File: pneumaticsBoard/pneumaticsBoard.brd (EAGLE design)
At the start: 188 x 25.4 mm, 48 parts, among them IC1 MAX232, Q1 BSS296, Q2 BSS296, Q3 BSS296, Q4 BSS296, Q5 BSS296, Q6 BSS296, Q7 BSS296, Q8 BSS296, U1 ATMEGA328P-PU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

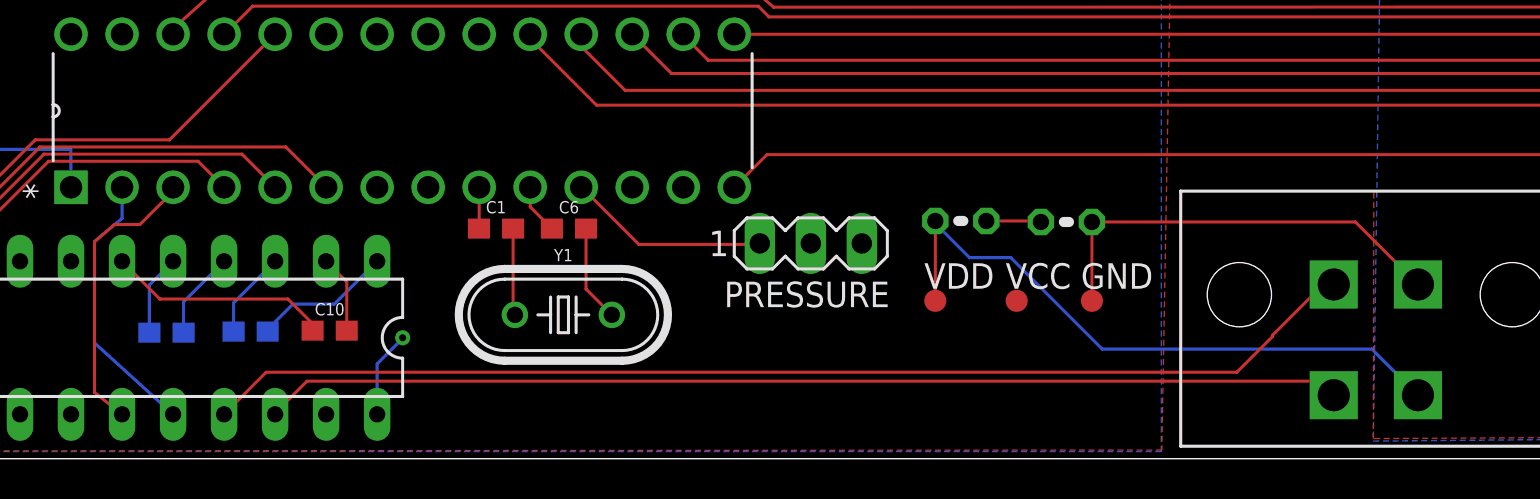
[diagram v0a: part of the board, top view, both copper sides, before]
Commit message: Pneumatics Board complete. Gerber files uploaded.
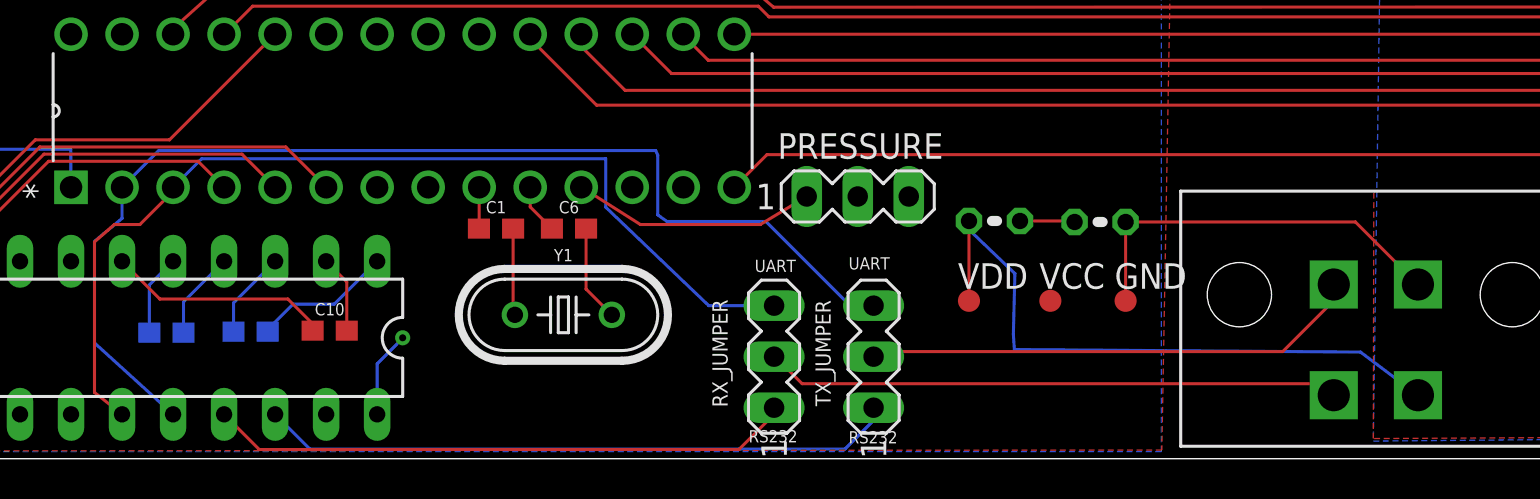
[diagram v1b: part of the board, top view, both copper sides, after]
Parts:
- added RX_JUMPER, TX_JUMPER: (no value), con-lstb:MA03-1
- moved PRESSURE 3.30 mm to (62.0, 13.1)
- moved GND 1.68 mm to (75.3, 7.86)
- moved R4 1.68 mm to (68.8, 11.8)
- moved R6 1.68 mm to (74.0, 11.8)
- moved VCC 1.68 mm to (71.5, 7.86)
- moved VDD 1.68 mm to (67.5, 7.86)
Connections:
- removed net RS232_RX-ATMEGA_TX: IC1.12, U1.2
- removed net RS232_TX-ATMEGA_RX: IC1.11, U1.3
- new net N$16: IC1.13, RX_JUMPER.1
- new net RX_ORIGINAL: RX_JUMPER.2, U$2.P1
- new net TX_ORIGINAL: TX_JUMPER.2, U$2.P3
- net N$3: now also IC1.14, TX_JUMPER.1; no longer R4.1, R6.2
- net RX: now also IC1.12, TX_JUMPER.3, U1.2; no longer IC1.13, U$2.P3
- net TX: now also IC1.11, RX_JUMPER.3, U1.3; no longer IC1.14, U$2.P1
- net VCC: now also R4.1, R6.2
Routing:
- net N$16: track 0.00 -> 29.2 mm
- net N$3: track 2.74 -> 31.7 mm
- net RX_ORIGINAL: track 0.00 -> 28.7 mm
- net TX_ORIGINAL: track 0.00 -> 24.9 mm
- net RS232_TX-ATMEGA_RX: track 14.4 -> 0.00 mm
- net RS232_RX-ATMEGA_TX: track 13.7 -> 0.00 mm
- net TX: track 53.7 -> 49.3 mm
- net VCC: track 4.31 -> 7.05 mm
- net N$6: track 10.1 -> 12.2 mm
- net GND: track 35.4 -> 33.7 mm
- net RX: track 58.0 -> 56.8 mm
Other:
- board text added: "RS232"
- board text added: "UART"

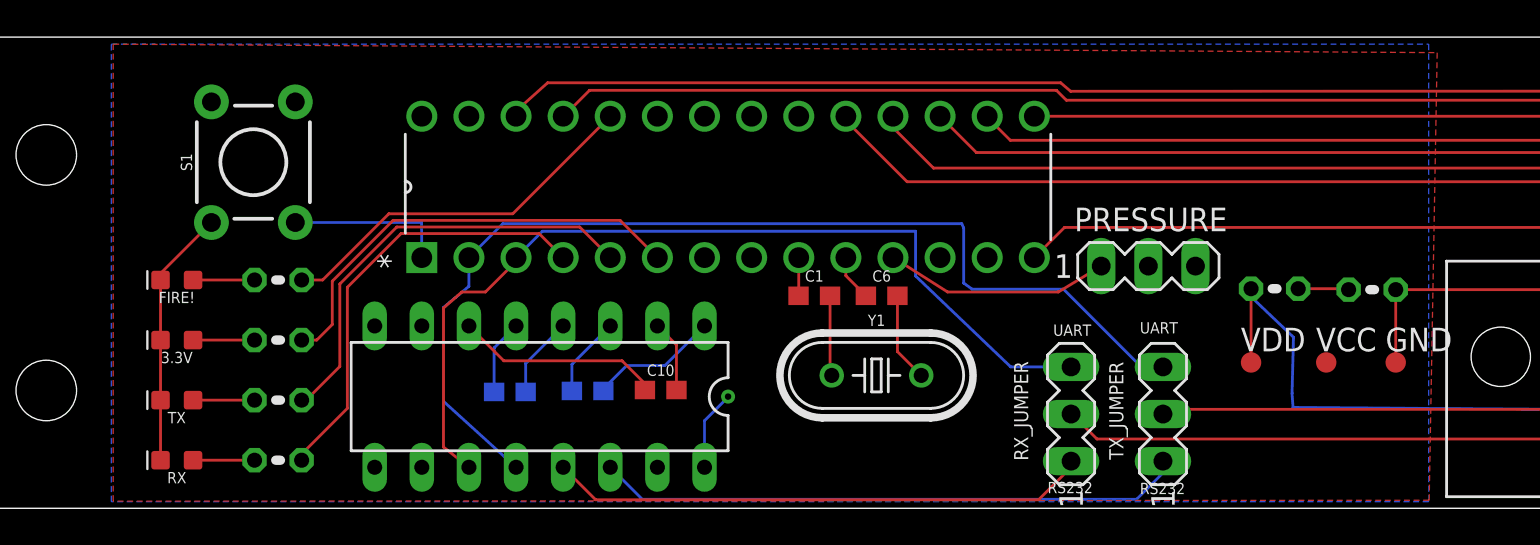
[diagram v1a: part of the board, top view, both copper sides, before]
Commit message: Moved C10, changed GND place on logic side.
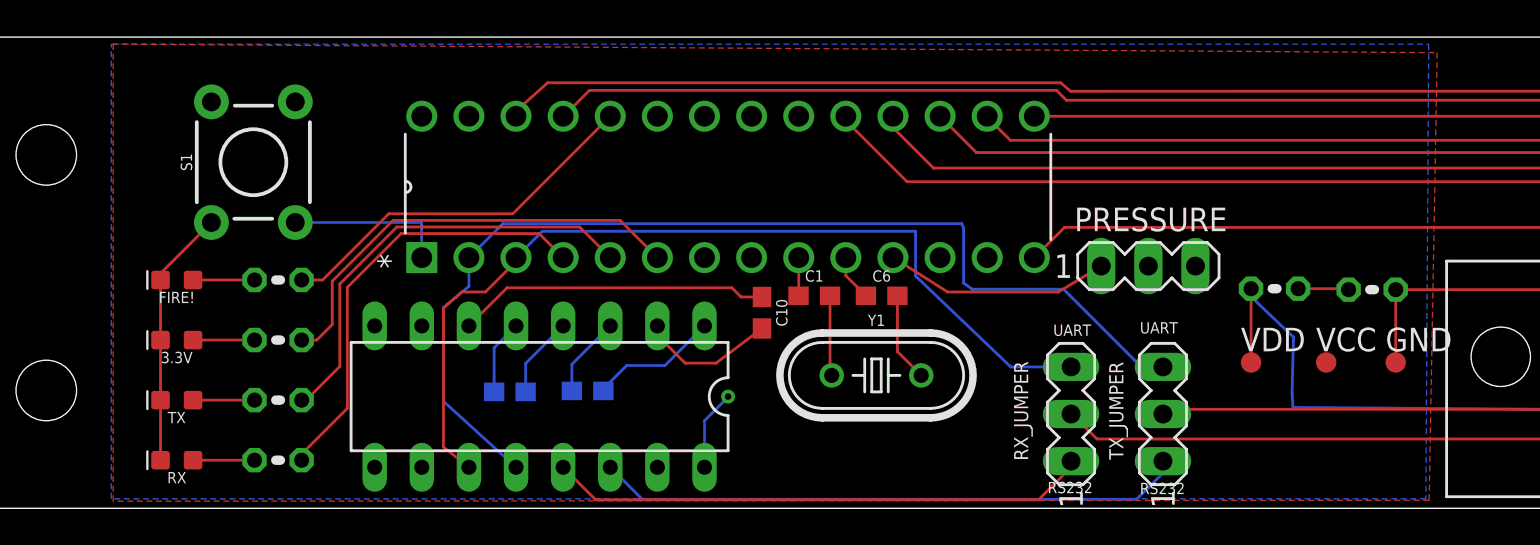
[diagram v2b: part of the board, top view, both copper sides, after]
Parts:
- moved C10 6.87 mm to (41.1, 10.5), turned to 270 degrees
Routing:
- net N$14: track 11.1 -> 16.9 mm
- net N$13: track 3.88 -> 7.39 mm
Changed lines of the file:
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@@
 <setting verticaltext="up"/>
 </settings>
-<grid distance="0.001" unitdist="inch" unit="inch" style="lines" multiple="1" display="yes" altdistance="5" altunitdist="mil" altunit="inch"/>
+<grid distance="0.006" unitdist="inch" unit="inch" style="lines" multiple="1" display="yes" altdistance="5" altunitdist="mil" altunit="inch"/>
 <layers>
 <layer number="1" name="Top" color="4" fill="1" visible="yes" active="yes"/>
@@
 <attribute name="OC_FARNELL" value="9723773" x="29.1338" y="6.0198" size="1.778" layer="27" rot="R180" display="off"/>
 <attribute name="OC_NEWARK" value="68K4544" x="29.1338" y="6.0198" size="1.778" layer="27" rot="R180" display="off"/>
-<attribute name="VALUE" x="39.5351" y="9.1948" size="1.27" layer="27" ratio="10" rot="R270"/>
+<attribute name="VALUE" x="39.5605" y="8.6614" size="1.27" layer="27" ratio="10" rot="R270"/>
 </element>
 <element name="S1" library="SparkFun-Switches" package="TACTILE_SWITCH_PTH_6.0MM" value="MOMENTARY-SWITCH-SPST-PTH-6.0MM" x="13.7033" y="18.6563" rot="R90">
@@
 <attribute name="PROD_ID" value="CAP-07884" x="27.5336" y="6.2738" size="1.778" layer="28" rot="MR0" display="off"/>
 </element>
-<element name="C10" library="SparkFun-Capacitors" package="0603" value="1uF" x="35.6616" y="6.3754">
-<attribute name="PROD_ID" value="CAP-07884" x="35.6616" y="6.3754" size="1.778" layer="27" display="off"/>
+<element name="C10" library="SparkFun-Capacitors" package="0603" value="1uF" x="41.1226" y="10.541" rot="R270">
+<attribute name="PROD_ID" value="CAP-07884" x="41.1226" y="10.541" size="1.778" layer="27" rot="R270" display="off"/>
 </element>
 <element name="C1" library="SparkFun-Capacitors" package="0603" value="22pF" x="43.942" y="11.4554">
@@
 <contactref element="IC1" pad="2"/>
 <contactref element="C10" pad="2"/>
-<wire x1="36.5116" y1="6.3754" x2="36.5116" y2="8.802" width="0.1524" layer="1"/>
-<wire x1="36.5116" y1="8.802" x2="35.4838" y2="9.8298" width="0.1524" layer="1"/>
+<wire x1="35.4838" y1="9.8298" x2="35.4838" y2="9.3218" width="0.1524" layer="1"/>
+<wire x1="35.4838" y1="9.3218" x2="36.9824" y2="7.8232" width="0.1524" layer="1"/>
+<wire x1="36.9824" y1="7.8232" x2="38.6452" y2="7.8232" width="0.1524" layer="1"/>
+<wire x1="38.6452" y1="7.8232" x2="41.1226" y2="9.691" width="0.1524" layer="1"/>
 </signal>
 <signal name="N$14">
 <contactref element="IC1" pad="6"/>
 <contactref element="C10" pad="1"/>
-<wire x1="34.8116" y1="6.3754" x2="34.8116" y2="6.7174" width="0.1524" layer="1"/>
-<wire x1="34.8116" y1="6.7174" x2="33.5788" y2="7.9502" width="0.1524" layer="1"/>
-<wire x1="33.5788" y1="7.9502" x2="27.2034" y2="7.9502" width="0.1524" layer="1"/>
-<wire x1="27.2034" y1="7.9502" x2="25.3238" y2="9.8298" width="0.1524" layer="1"/>
+<wire x1="41.1226" y1="11.391" x2="39.9932" y2="11.391" width="0.1524" layer="1"/>
+<wire x1="39.9932" y1="11.391" x2="39.497" y2="11.8872" width="0.1524" layer="1"/>
+<wire x1="39.497" y1="11.8872" x2="27.3812" y2="11.8872" width="0.1524" layer="1"/>
+<wire x1="27.3812" y1="11.8872" x2="25.3238" y2="9.8298" width="0.1524" layer="1"/>
 </signal>
 <signal name="GND">
@@
 <vertex x="6.0452" y="25.019"/>
 <vertex x="77.0636" y="25.019"/>
-<vertex x="77.0636" y="0.3556"/>
-<vertex x="6.0452" y="0.3556"/>
+<vertex x="76.9112" y="0.508"/>
+<vertex x="6.0452" y="0.508"/>
 </polygon>
 <contactref element="PRESSURE" pad="3"/>

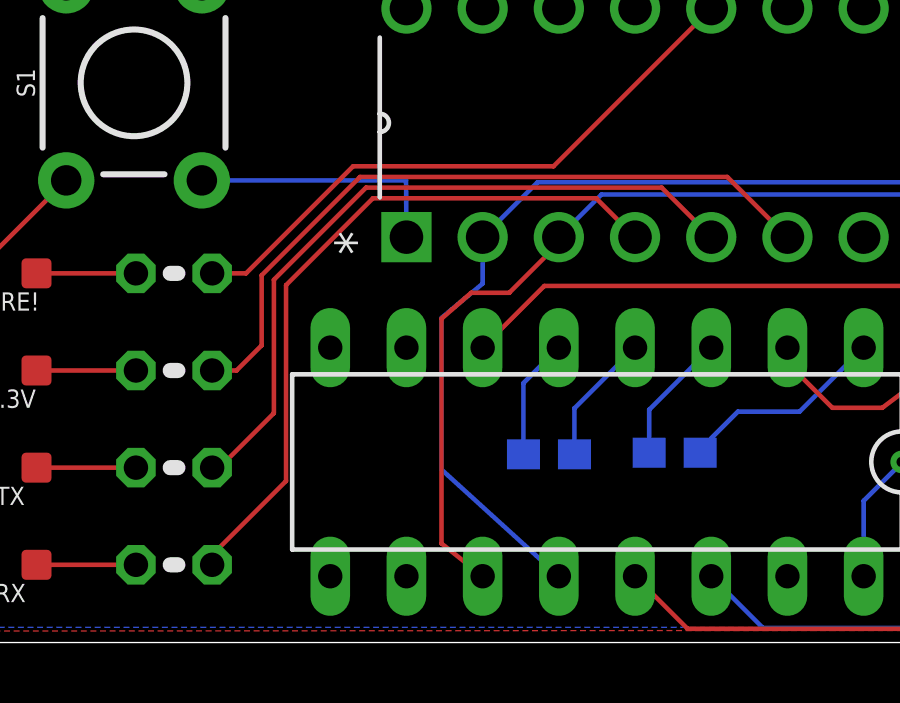
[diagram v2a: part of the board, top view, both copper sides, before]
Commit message: Added 0 Ohm Resistors on TX and RX lines just in case.
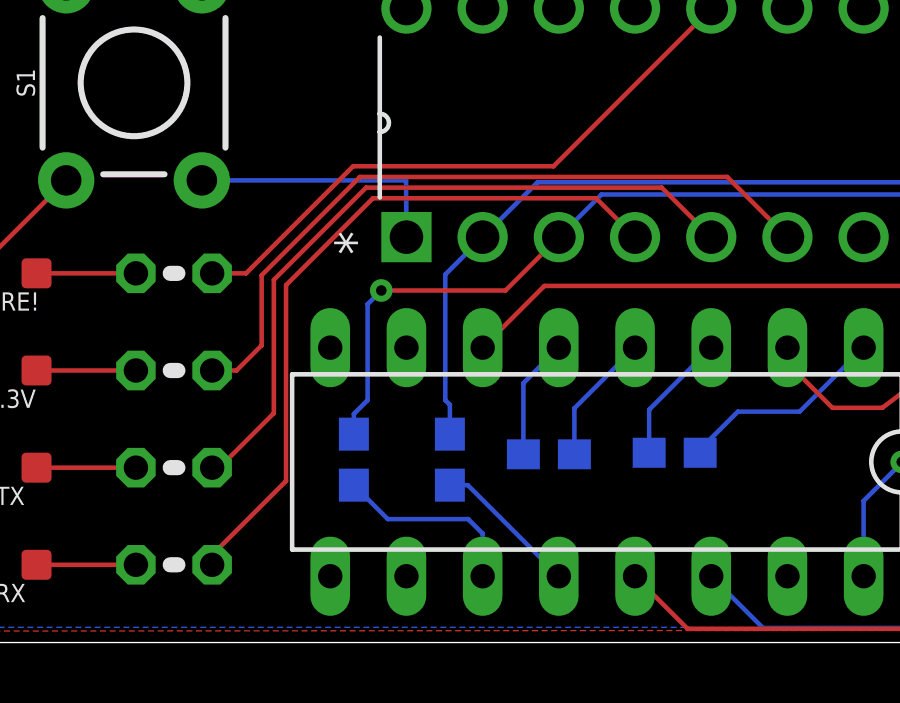
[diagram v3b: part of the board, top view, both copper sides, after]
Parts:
- added C2, C3: 1uF, SparkFun-Capacitors:0603
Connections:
- new net N$17: C2.1, IC1.11
- new net N$18: C3.1, IC1.12
- net RX: now also C3.2; no longer IC1.12
- net TX: now also C2.2; no longer IC1.11
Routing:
- net RX: track 56.8 -> 50.3 mm
- net N$17: track 0.00 -> 6.38 mm
- net N$18: track 0.00 -> 4.89 mm
- net TX: track 49.3 -> 46.7 mm, vias 0 -> 1
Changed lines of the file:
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@@
 <attribute name="VALUE" x="60.706" y="1.27" size="1.27" layer="27" ratio="10" rot="R90"/>
+</element>
+<element name="C2" library="SparkFun-Capacitors" package="0603" value="1uF" x="21.0312" y="6.096" rot="MR90">
+<attribute name="PROD_ID" value="CAP-07884" x="21.0312" y="6.096" size="1.778" layer="28" rot="MR90" display="off"/>
+</element>
+<element name="C3" library="SparkFun-Capacitors" package="0603" value="1uF" x="24.2316" y="6.096" rot="MR90">
+<attribute name="PROD_ID" value="CAP-07884" x="24.2316" y="6.096" size="1.778" layer="28" rot="MR90" display="off"/>
 </element>
 </elements>
@@
 </signal>
 <signal name="RX">
-<contactref element="IC1" pad="12"/>
 <contactref element="U1" pad="2"/>
 <contactref element="TX_JUMPER" pad="3"/>
-<wire x1="25.3238" y1="13.5128" x2="25.3238" y2="11.9634" width="0.1524" layer="16"/>
-<wire x1="25.3238" y1="11.9634" x2="23.9522" y2="10.8204" width="0.1524" layer="16"/>
-<wire x1="23.9522" y1="10.8204" x2="23.9522" y2="5.7658" width="0.1524" layer="16"/>
-<wire x1="23.9522" y1="5.7658" x2="27.8638" y2="2.2098" width="0.1524" layer="16"/>
 <wire x1="62.738" y1="7.62" x2="61.5696" y2="7.62" width="0.1524" layer="16"/>
 <wire x1="61.5696" y1="7.62" x2="57.3786" y2="11.811" width="0.1524" layer="16"/>
@@
 <wire x1="51.9938" y1="15.113" x2="51.8922" y2="15.3416" width="0.1524" layer="16"/>
 <wire x1="51.8922" y1="15.3416" x2="27.1526" y2="15.3416" width="0.1524" layer="16"/>
-<wire x1="27.1526" y1="15.3416" x2="25.3238" y2="13.5128" width="0.1524" layer="16"/>
+<wire x1="25.3238" y1="13.5128" x2="27.1526" y2="15.3416" width="0.1524" layer="16"/>
+<contactref element="C3" pad="2"/>
+<wire x1="24.2316" y1="6.946" x2="24.2316" y2="7.9248" width="0.1524" layer="16"/>
+<wire x1="24.2316" y1="7.9248" x2="24.0792" y2="8.0772" width="0.1524" layer="16"/>
+<wire x1="24.0792" y1="8.0772" x2="24.0792" y2="12.2682" width="0.1524" layer="16"/>
+<wire x1="24.0792" y1="12.2682" x2="25.3238" y2="13.5128" width="0.1524" layer="16"/>
 </signal>
 <signal name="RESET">
@@
 </signal>
 <signal name="TX">
-<contactref element="IC1" pad="11"/>
 <contactref element="U1" pad="3"/>
 <contactref element="RX_JUMPER" pad="3"/>
-<wire x1="27.8638" y1="13.5128" x2="27.8638" y2="13.3096" width="0.1524" layer="1"/>
-<wire x1="27.8638" y1="13.3096" x2="26.2128" y2="11.6586" width="0.1524" layer="1"/>
-<wire x1="26.2128" y1="11.6586" x2="24.9428" y2="11.6586" width="0.1524" layer="1"/>
-<wire x1="24.9428" y1="11.6586" x2="23.9522" y2="10.795" width="0.1524" layer="1"/>
-<wire x1="23.9522" y1="10.795" x2="23.9522" y2="3.302" width="0.1524" layer="1"/>
-<wire x1="23.9522" y1="3.302" x2="25.3238" y2="2.2098" width="0.1524" layer="1"/>
 <wire x1="57.785" y1="7.62" x2="54.5338" y2="7.62" width="0.1524" layer="16"/>
 <wire x1="54.5338" y1="7.62" x2="49.403" y2="12.5222" width="0.1524" layer="16"/>
@@
 <wire x1="49.403" y1="14.9352" x2="29.2862" y2="14.9352" width="0.1524" layer="16"/>
 <wire x1="29.2862" y1="14.9352" x2="27.8638" y2="13.5128" width="0.1524" layer="16"/>
+<contactref element="C2" pad="2"/>
+<wire x1="21.0312" y1="6.946" x2="21.0312" y2="7.62" width="0.1524" layer="16"/>
+<wire x1="21.0312" y1="7.62" x2="21.4884" y2="8.0772" width="0.1524" layer="16"/>
+<wire x1="21.4884" y1="8.0772" x2="21.4884" y2="11.2776" width="0.1524" layer="16"/>
+<via x="21.9456" y="11.7348" extent="1-16" drill="0.35"/>
+<wire x1="21.9456" y1="11.7348" x2="26.0858" y2="11.7348" width="0.1524" layer="1"/>
+<wire x1="26.0858" y1="11.7348" x2="27.8638" y2="13.5128" width="0.1524" layer="1"/>
+<wire x1="21.4884" y1="11.2776" x2="21.9456" y2="11.7348" width="0.1524" layer="16"/>
+</signal>
+<signal name="N$17">
+<contactref element="IC1" pad="11"/>
+<contactref element="C2" pad="1"/>
+<wire x1="25.3238" y1="2.2098" x2="25.3238" y2="3.6322" width="0.1524" layer="16"/>
+<wire x1="24.8412" y1="4.1148" x2="22.1624" y2="4.1148" width="0.1524" layer="16"/>
+<wire x1="22.1624" y1="4.1148" x2="21.0312" y2="5.246" width="0.1524" layer="16"/>
+<wire x1="25.3238" y1="3.6322" x2="24.8412" y2="4.1148" width="0.1524" layer="16"/>
+</signal>
+<signal name="N$18">
+<contactref element="IC1" pad="12"/>
+<contactref element="C3" pad="1"/>
+<wire x1="24.2316" y1="5.246" x2="24.8276" y2="5.246" width="0.1524" layer="16"/>
+<wire x1="24.8276" y1="5.246" x2="27.8638" y2="2.2098" width="0.1524" layer="16"/>
 </signal>
 </signals>
